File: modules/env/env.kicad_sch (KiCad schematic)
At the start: 29 parts, among them SW1 GATE MODE SELECT, SW2 ALGO MODE SELECT, U1 MCP6002-xSN, U2 ATtiny1616-M, U3 MCP6002-xSN

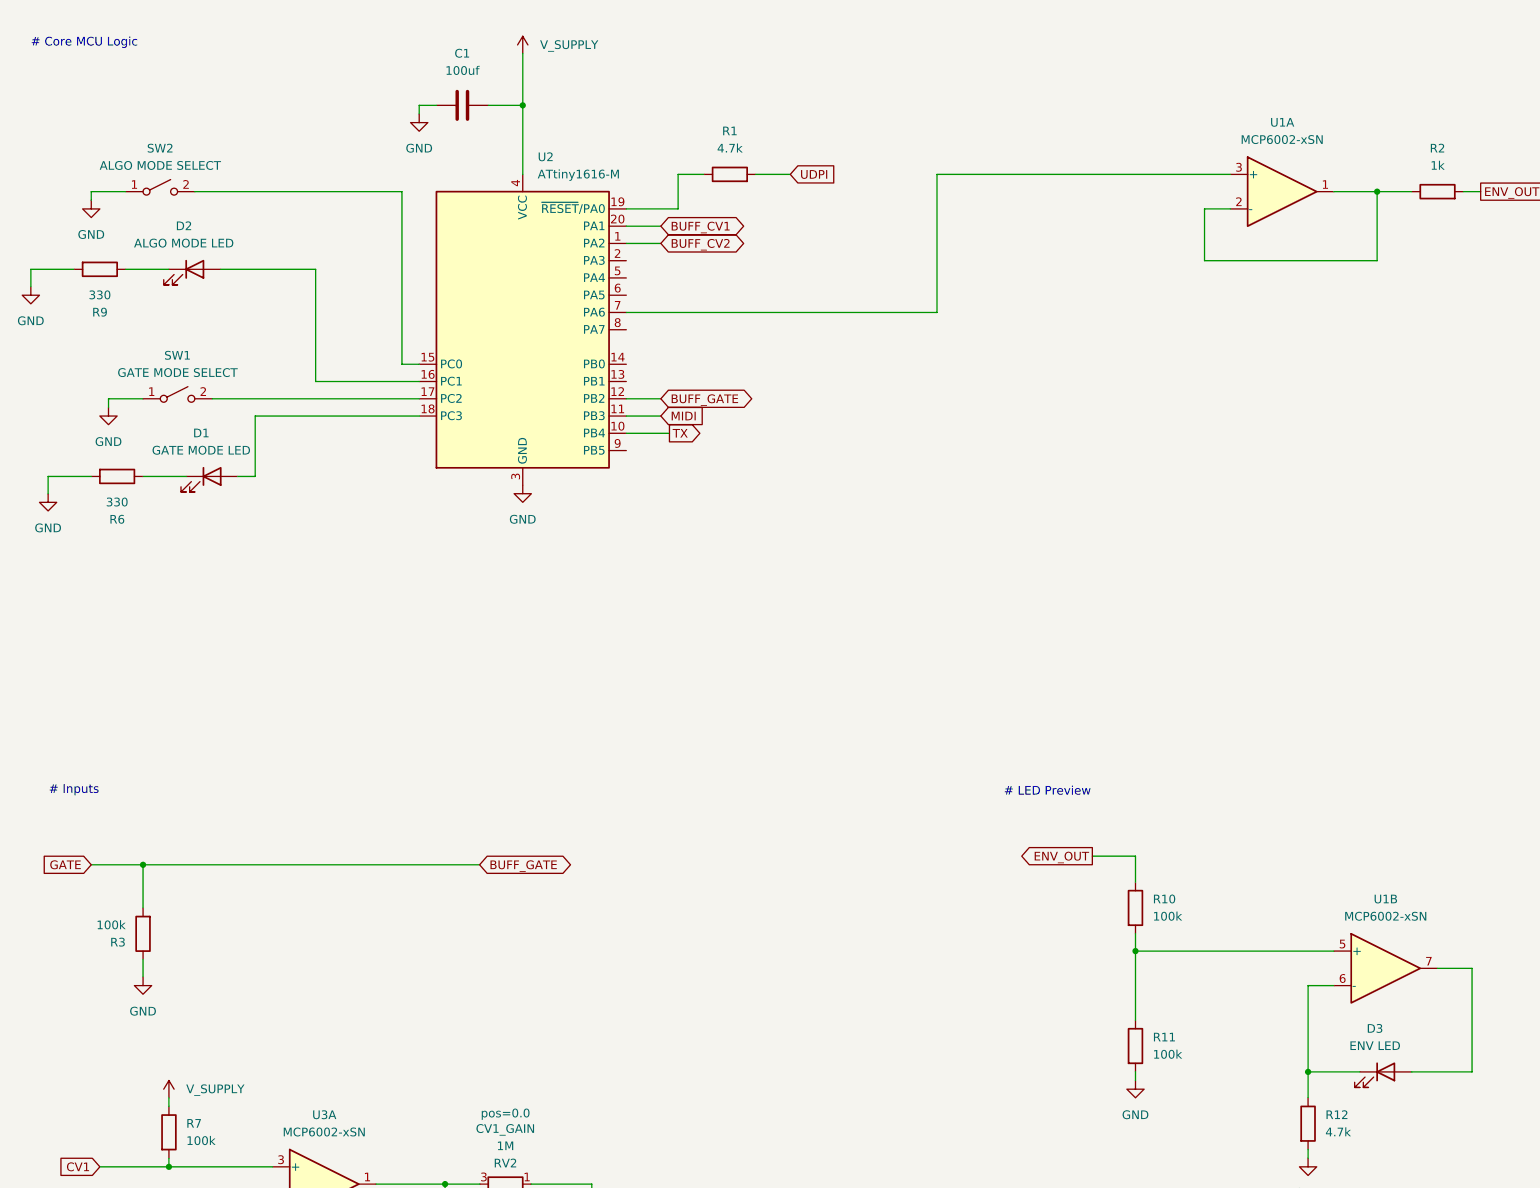
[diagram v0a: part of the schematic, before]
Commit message: env: introduce envelope generator. This is a digital envelope generator which has multiple modes to support different needs. Currently it has three modes/algorithms It also support MIDI and as well as usual Gate & CV
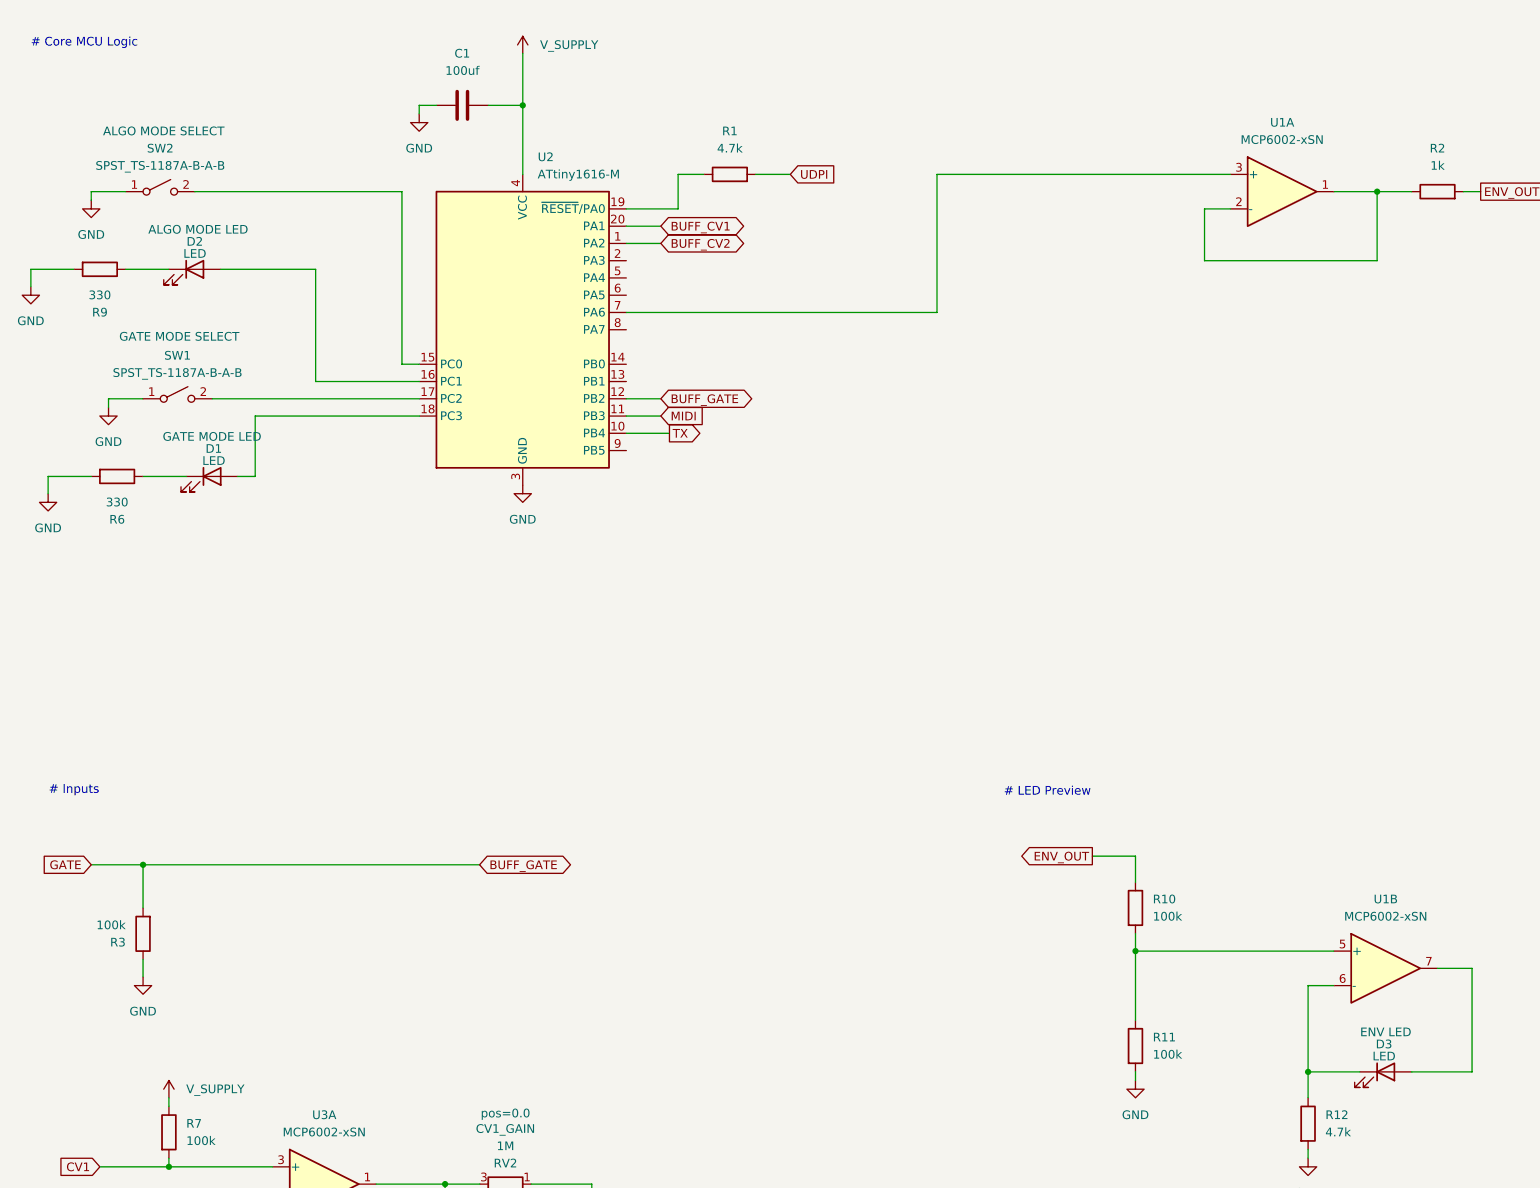
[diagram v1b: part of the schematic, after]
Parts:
- D1: value GATE MODE LED -> LED; Comment (none) -> GATE MODE LED
- D2: value ALGO MODE LED -> LED; Comment (none) -> ALGO MODE LED
- D3: value ENV LED -> LED; Comment (none) -> ENV LED
- SW1: value GATE MODE SELECT -> SPST_TS-1187A-B-A-B; Comment (none) -> GATE MODE SELECT
- SW2: value ALGO MODE SELECT -> SPST_TS-1187A-B-A-B; Comment (none) -> ALGO MODE SELECT
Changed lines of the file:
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@@
 		(on_board yes)
 		(dnp no)
-		(fields_autoplaced yes)
 		(property "Reference" "SW1"
 			(at 41.91 76.2 0)
@@
 			)
 		)
-		(property "Value" "GATE MODE SELECT"
+		(property "Value" "SPST_TS-1187A-B-A-B"
 			(at 41.91 78.74 0)
 			(effects
@@
 			)
 		)
+		(property "Comment" "GATE MODE SELECT"
+			(at 42.164 73.406 0)
+			(effects
+				(font
+					(size 1.27 1.27)
+				)
+			)
+		)
 		(pin "1"
 		)
@@
 		(on_board yes)
 		(dnp no)
-		(fields_autoplaced yes)
 		(property "Reference" "D1"
-			(at 45.4025 87.63 0)
-			(effects
-				(font
-					(size 1.27 1.27)
-				)
-			)
-		)
-		(property "Value" "GATE MODE LED"
-			(at 45.4025 90.17 0)
+			(at 47.244 89.916 0)
+			(effects
+				(font
+					(size 1.27 1.27)
+				)
+			)
+		)
+		(property "Value" "LED"
+			(at 47.244 91.694 0)
 			(effects
 				(font
@@
 				)
 				(hide yes)
+			)
+		)
+		(property "Comment" "GATE MODE LED"
+			(at 46.99 88.138 0)
+			(effects
+				(font
+					(size 1.27 1.27)
+				)
 			)
 		)
@@
 		(on_board yes)
 		(dnp no)
-		(fields_autoplaced yes)
 		(property "Reference" "D3"
-			(at 218.1225 175.26 0)
-			(effects
-				(font
-					(size 1.27 1.27)
-				)
-			)
-		)
-		(property "Value" "ENV LED"
-			(at 218.1225 177.8 0)
+			(at 219.456 177.546 0)
+			(effects
+				(font
+					(size 1.27 1.27)
+				)
+			)
+		)
+		(property "Value" "LED"
+			(at 219.456 179.324 0)
 			(effects
 				(font
@@
 				)
 				(hide yes)
+			)
+		)
+		(property "Comment" "ENV LED"
+			(at 219.71 175.768 0)
+			(effects
+				(font
+					(size 1.27 1.27)
+				)
 			)
 		)
@@
 		(on_board yes)
 		(dnp no)
-		(fields_autoplaced yes)
 		(property "Reference" "D2"
-			(at 42.8625 57.15 0)
-			(effects
-				(font
-					(size 1.27 1.27)
-				)
-			)
-		)
-		(property "Value" "ALGO MODE LED"
-			(at 42.8625 59.69 0)
+			(at 44.45 59.436 0)
+			(effects
+				(font
+					(size 1.27 1.27)
+				)
+			)
+		)
+		(property "Value" "LED"
+			(at 44.45 61.214 0)
 			(effects
 				(font
@@
 				)
 				(hide yes)
+			)
+		)
+		(property "Comment" "ALGO MODE LED"
+			(at 44.958 57.658 0)
+			(effects
+				(font
+					(size 1.27 1.27)
+				)
 			)
 		)
@@
 		(on_board yes)
 		(dnp no)
-		(fields_autoplaced yes)
 		(property "Reference" "SW2"
 			(at 39.37 45.72 0)
@@
 			)
 		)
-		(property "Value" "ALGO MODE SELECT"
+		(property "Value" "SPST_TS-1187A-B-A-B"
 			(at 39.37 48.26 0)
 			(effects
@@
 			)
 		)
+		(property "Comment" "ALGO MODE SELECT "
+			(at 39.878 43.18 0)
+			(effects
+				(font
+					(size 1.27 1.27)
+				)
+			)
+		)

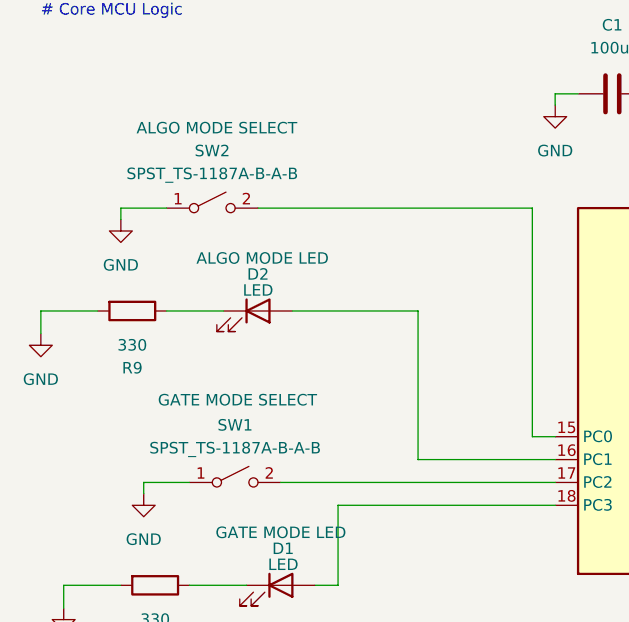
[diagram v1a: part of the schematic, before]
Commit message: Use a better button
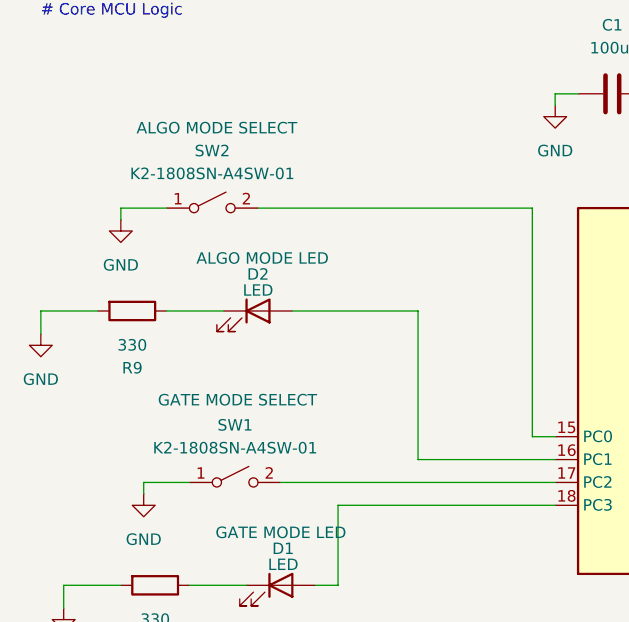
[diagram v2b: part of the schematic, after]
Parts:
- SW1, SW2: value SPST_TS-1187A-B-A-B -> K2-1808SN-A4SW-01; footprint BreadModular_MISC:SPST_TS-1187A-B-A-B -> BreadModular_MISC:K2-1808SN-A4SW-01
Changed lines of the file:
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@@
 			)
 		)
-		(property "Value" "SPST_TS-1187A-B-A-B"
+		(property "Value" "K2-1808SN-A4SW-01"
 			(at 41.91 78.74 0)
 			(effects
@@
 			)
 		)
-		(property "Footprint" "BreadModular_MISC:SPST_TS-1187A-B-A-B"
+		(property "Footprint" "BreadModular_MISC:K2-1808SN-A4SW-01"
 			(at 41.91 82.55 0)
 			(effects
@@
 			)
 		)
-		(property "Value" "SPST_TS-1187A-B-A-B"
+		(property "Value" "K2-1808SN-A4SW-01"
 			(at 39.37 48.26 0)
 			(effects
@@
 			)
 		)
-		(property "Footprint" "BreadModular_MISC:SPST_TS-1187A-B-A-B"
+		(property "Footprint" "BreadModular_MISC:K2-1808SN-A4SW-01"
 			(at 39.37 52.07 0)
 			(effects
